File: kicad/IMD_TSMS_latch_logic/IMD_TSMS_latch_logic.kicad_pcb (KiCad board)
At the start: 2 copper layers, 105.5 x 67 mm, 81 parts, among them IC1 NE555, J1 Conn_01x02, J3 Conn_01x02, J4 Conn_01x02, J5 Conn_01x02, J6 Conn_01x02, J7 Conn_01x02, J8 Conn_01x02, J9 Conn_01x02, K1 SANYOU_SRD_Form_C, K2 SANYOU_SRD_Form_C, Q2 AO3400A, Q3 AO3401A, Q5 AO3401A, Q6 AO3401A, SW1 SW_Push, U1 4001, U2 4009, U3 4009, U4 4001, U5 LTV-817S, U6 LM311

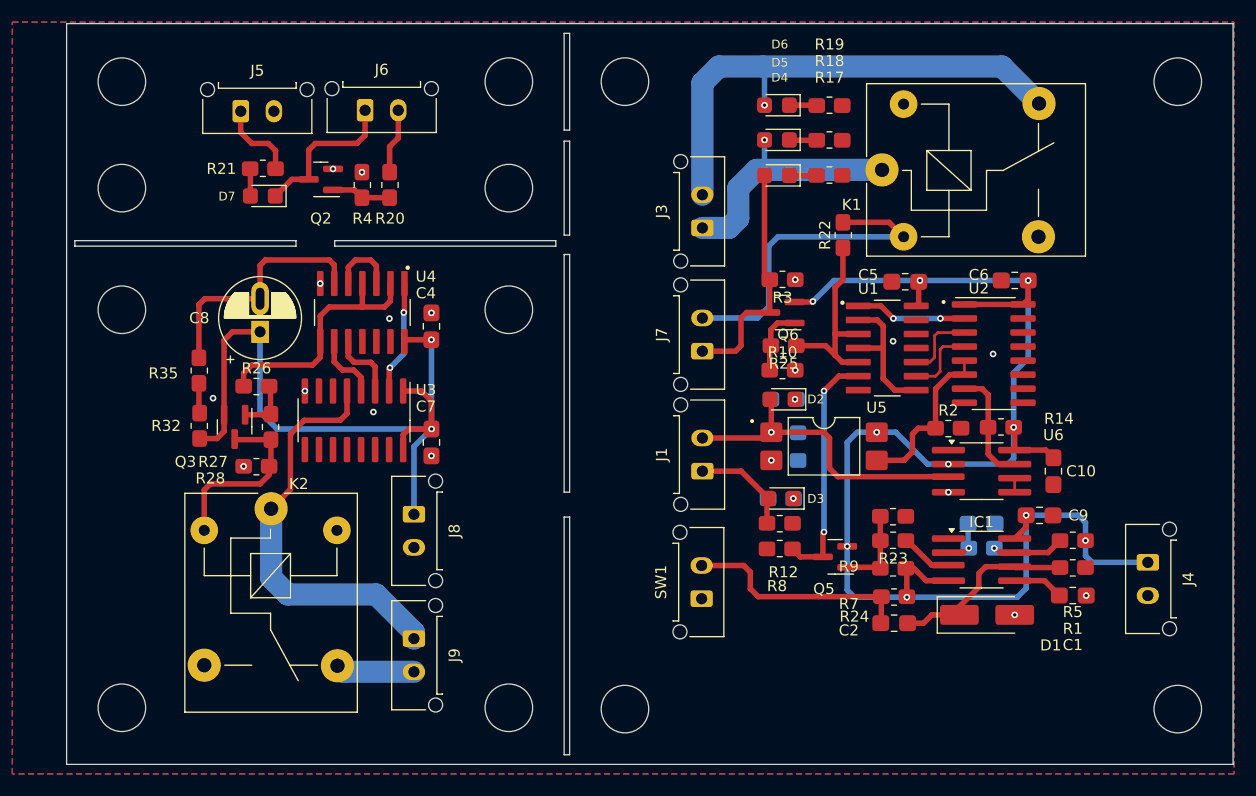
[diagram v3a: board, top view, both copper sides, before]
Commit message: Update IMD_TSMS latch PCB layout and generate Gerbers
Updated the IMD_TSMS_latch_logic PCB layout with multiple component position changes, replaced R32 with D1 (diode), and removed R35. Adjusted mounting hole and connector locations, and generated new Gerber files in the gerber_latch directory. Also removed old backup files from VCU V3.2.
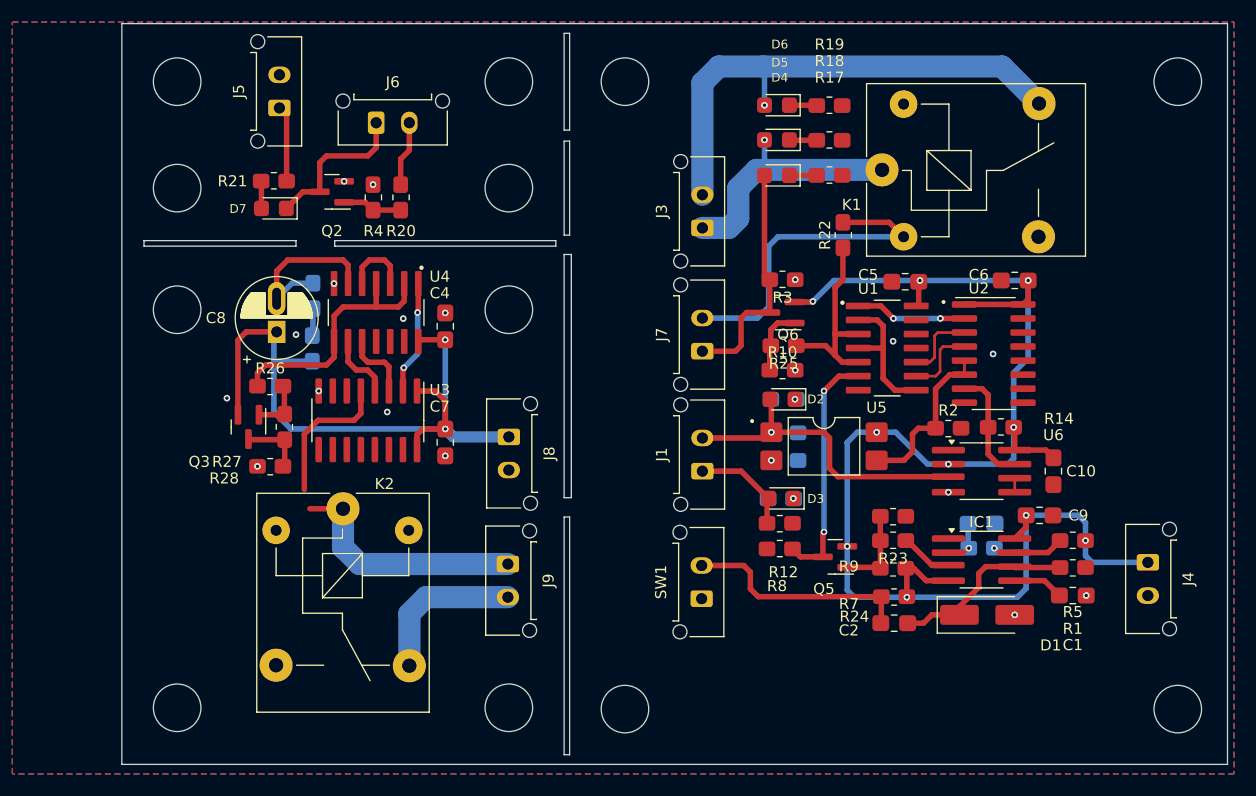
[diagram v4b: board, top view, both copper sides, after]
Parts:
- R32, R35: moved to B.Cu
- moved R32 12.4 mm to (97.2, 99.5)
- moved R35 12.3 mm to (97.2, 94.8)
- moved J8 11.1 mm to (115.0, 107.5)
- moved J9 10.9 mm to (114.9, 119.0)
- moved K2 6.50 mm to (100.0, 114.0)
- moved H11 5.00 mm to (85.0, 85.0)
- moved H7 5.00 mm to (85.0, 132.0)
- moved H8 5.00 mm to (85.0, 75.4)
- moved H9 5.00 mm to (85.0, 96.0)
- moved J5 3.51 mm to (94.2, 77.8), turned to 90 degrees
- moved D7 1.51 mm to (93.8, 86.8)
- moved J6 1.51 mm to (103.0, 79.1)
- moved Q2 1.51 mm to (99.0, 85.3)
- moved R20 1.51 mm to (105.2, 85.8)
- moved R21 1.51 mm to (93.8, 84.3)
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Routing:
- net Net-(Q3-D): track 16.6 -> 6.67 mm
- net /TSMS_output: track 7.14 -> 14.2 mm
- net /TSMS_reset: track 22.3 -> 15.3 mm
- net +12V: track 206.0 -> 203.0 mm
- net /TSMS_input: track 37.2 -> 35.0 mm
- net GND: vias 17 -> 19
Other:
- board size 105.5 x 67 mm -> 100 x 67 mm

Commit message: pcb layout update
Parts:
- removed Q5: AO3401A, RMC_SOT:SOT-23
- removed R23, R7: 1k, RMC_Resistor:R_0805_2012Metric_Pad1.20x1.40mm_HandSolder_L
- removed R8: 10k, RMC_Resistor:R_0805_2012Metric_Pad1.20x1.40mm_HandSolder_L
- removed R9: 100k, RMC_Resistor:R_0805_2012Metric_Pad1.20x1.40mm_HandSolder_L
- added Q1: NMOS, Package_TO_SOT_SMD:SOT-23, F.Cu at (138.8, 126.6)
- added Q4: NMOS, Package_TO_SOT_SMD:SOT-23, F.Cu at (157.1, 127.0)
- added R29: 1k, Resistor_SMD:R_0805_2012Metric_Pad1.20x1.40mm_HandSolder, F.Cu at (139.5, 117.6)
- added R30: 1k, Resistor_SMD:R_0805_2012Metric_Pad1.20x1.40mm_HandSolder, F.Cu at (142.4, 124.4)
- added R31: 1k, Resistor_SMD:R_0805_2012Metric_Pad1.20x1.40mm_HandSolder, F.Cu at (152.2, 118.3)
- added R33: 1k, Resistor_SMD:R_0805_2012Metric_Pad1.20x1.40mm_HandSolder, F.Cu at (150.8, 127.7)
- C1, C10, C4, C5, C6, C7: footprint RMC_Capacitor:C_0805_2012Metric_Pad1.18x1.45mm_HandSolder_L -> Capacitor_SMD:C_0805_2012Metric_Pad1.18x1.45mm_HandSolder
- C2: value 100n -> 1u; footprint RMC_Capacitor:C_0805_2012Metric_Pad1.18x1.45mm_HandSolder_L -> Capacitor_SMD:C_0805_2012Metric_Pad1.18x1.45mm_HandSolder
- C3: footprint RMC_Capacitor:C_0805_2012Metric_Pad1.18x1.45mm_HandSolder_L -> Capacitor_SMD:C_0805_2012Metric_Pad1.18x1.45mm_HandSolder; moved to F.Cu
- C8: footprint RMC_Capacitor:CP_Radial_D6.3mm_P2.50mm_extended -> Capacitor_THT:CP_Radial_D6.3mm_P2.50mm
- C9: footprint RMC_Capacitor:C_0805_2012Metric_Pad1.18x1.45mm_HandSolder_L -> Capacitor_SMD:C_0805_2012Metric_Pad1.18x1.45mm_HandSolder; moved to B.Cu
- D1: value D -> SS34; footprint Diode_SMD:D_SMA_Handsoldering -> extra_footprints:SS34 (1N5822)
- D2, D3, D4, D5, D6, D7: footprint RMC_LED:LED_0805_2012Metric_Pad1.45x1.40mm_HandSolder -> LED_SMD:LED_0805_2012Metric_Pad1.15x1.40mm_HandSolder
- IC1, U6: footprint RMC_SO:SOIC-8_3.9x4.9mm_P1.27mm_RMC_Handsolder -> Package_SO:SOIC-8_3.9x4.9mm_P1.27mm
- Q2, Q3, Q6: footprint RMC_SOT:SOT-23 -> Package_TO_SOT_SMD:SOT-23
- R1, R10, R11, R12, R13, R14, R15, R16, R17, R18, R19, R2, R20, R21, R22, R25, R26, R27, R28, R3, R32, R35, R4: footprint RMC_Resistor:R_0805_2012Metric_Pad1.20x1.40mm_HandSolder_L -> Resistor_SMD:R_0805_2012Metric_Pad1.20x1.40mm_HandSolder
- R24: value 10k -> 1k; footprint RMC_Resistor:R_0805_2012Metric_Pad1.20x1.40mm_HandSolder_L -> Resistor_SMD:R_0805_2012Metric_Pad1.20x1.40mm_HandSolder
- R5, R6: value 22k -> 10k; footprint RMC_Resistor:R_0805_2012Metric_Pad1.20x1.40mm_HandSolder_L -> Resistor_SMD:R_0805_2012Metric_Pad1.20x1.40mm_HandSolder
- U1, U4: footprint RMC_SO:SOIC127P600X175-14N -> RMC-KiCad:SOIC127P600X175-14N
- U2, U3: footprint RMC_SO:SOIC-16_3.9x9.9mm_P1.27mm_Handsolder -> Package_SO:SOIC-16_3.9x9.9mm_P1.27mm
- moved R1 21.6 mm to (146.6, 128.8), turned to -90 degrees
- moved R24 16.6 mm to (134.6, 128.6), turned to 90 degrees
- moved D1 9.67 mm to (154.3, 132.4)
- moved C3 8.92 mm to (164.7, 121.0)
- moved R6 7.73 mm to (153.4, 124.0), turned to 0 degrees
- moved C1 4.87 mm to (162.0, 124.7)
- moved C2 4.48 mm to (145.5, 125.5)
- moved C9 3.88 mm to (159.5, 116.2), turned to 180 degrees
- moved R5 2.51 mm to (163.7, 117.9), turned to -90 degrees
- moved C10 1.89 mm to (164.6, 108.7), turned to 0 degrees
- moved IC1 1.59 mm to (158.5, 120.0)
- moved J4 1.34 mm to (173.8, 118.0)
- moved SW1 0.06 mm to (132.4, 122.1)
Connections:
- C2 pad 1: Net-(C2-Pad1) -> Net-(Q1-D)
- C2 pad 2: /THRES -> Net-(C2-Pad2)
- C3 pad 1: /TRIG -> /DISCH
- IC1 pad 3: /fall_edge_out -> /IMD_reset
- IC1 pad 4: +12V -> Net-(IC1-RESET)
- IC1 pad 6: /THRES -> /DISCH
- R1 pad 1: /THRES -> Net-(C2-Pad2)
- R24 pad 1: Net-(C2-Pad1) -> GND
- R24 pad 2: +12V -> Net-(Q1-G)
- R6 pad 1: /DISCH -> +12V
- R6 pad 2: /TRIG -> Net-(IC1-RESET)
- SW1 pad 1: GND -> Net-(Q1-G)
- SW1 pad 2: Net-(C2-Pad1) -> +12V
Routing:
- net +12V: track 203.0 -> 272.2 mm, vias 12 -> 10
- net Net-(C2-Pad1): track 20.7 -> 0.00 mm
- net /THRES: track 17.1 -> 0.00 mm
- net /IMD_reset: track 21.7 -> 38.1 mm
- net Net-(C2-Pad2): track 0.00 -> 10.7 mm
- net /TRIG: track 4.25 -> 14.4 mm, vias 1 -> 0
- net Net-(Q1-G): track 0.00 -> 9.80 mm
- net Net-(Q5-G): track 7.73 -> 0.00 mm
- net Net-(Q1-D): track 0.00 -> 6.70 mm
- net Net-(Q3-D): track 6.67 -> 12.6 mm
- net /fall_edge_out: track 4.76 -> 0.00 mm
- net Net-(Q4-G): track 0.00 -> 4.44 mm
- net GND: track 0.00 -> 4.06 mm, vias 19 -> 18
- net Net-(IC1-RESET): track 0.00 -> 3.37 mm, vias 0 -> 1
- net /TSMS_input: track 35.0 -> 36.8 mm
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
